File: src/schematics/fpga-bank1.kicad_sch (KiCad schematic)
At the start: 7 parts

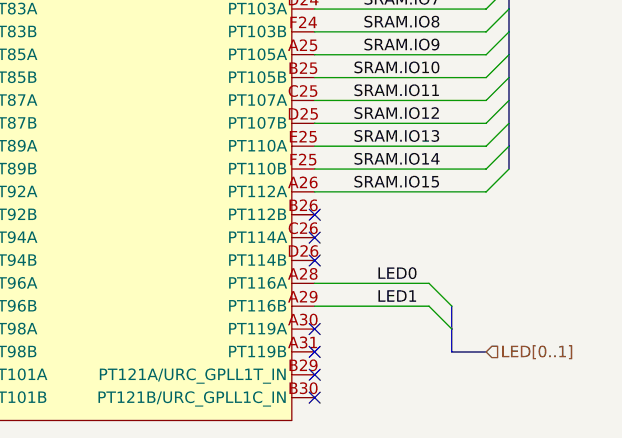
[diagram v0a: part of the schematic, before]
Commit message: Add footprint for the io connector
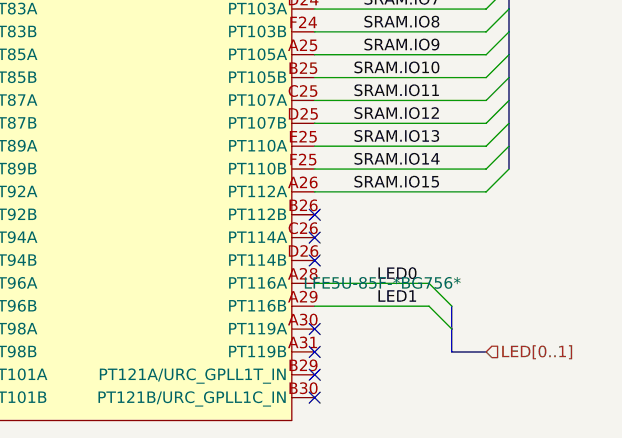
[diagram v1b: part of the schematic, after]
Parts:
- U6: value ~ -> LFE5U-85F-*BG756*
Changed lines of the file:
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@@
 			)
 		)
-		(property "Value" "~"
+		(property "Value" "LFE5U-85F-*BG756*"
 			(at 171.45 133.35 0)
 			(effects

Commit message: Add remaining component footprints (#79)
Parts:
- C54, C55, C56, C57, C58, C59: footprint (none) -> Capacitor_SMD:C_0402_1005Metric
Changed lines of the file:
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@@
 			)
 		)
-		(property "Footprint" ""
+		(property "Footprint" "Capacitor_SMD:C_0402_1005Metric"
 			(at 109.22 35.56 0)
 			(effects
@@
 			)
 		)
-		(property "Footprint" ""
+		(property "Footprint" "Capacitor_SMD:C_0402_1005Metric"
 			(at 161.29 35.56 0)
 			(effects
@@
 			)
 		)
-		(property "Footprint" ""
+		(property "Footprint" "Capacitor_SMD:C_0402_1005Metric"
 			(at 129.54 35.56 0)
 			(effects
@@
 			)
 		)
-		(property "Footprint" ""
+		(property "Footprint" "Capacitor_SMD:C_0402_1005Metric"
 			(at 139.7 35.56 0)
 			(effects
@@
 			)
 		)
-		(property "Footprint" ""
+		(property "Footprint" "Capacitor_SMD:C_0402_1005Metric"
 			(at 119.38 35.56 0)
 			(effects
@@
 			)
 		)
-		(property "Footprint" ""
+		(property "Footprint" "Capacitor_SMD:C_0402_1005Metric"
 			(at 149.86 35.56 0)
 			(effects

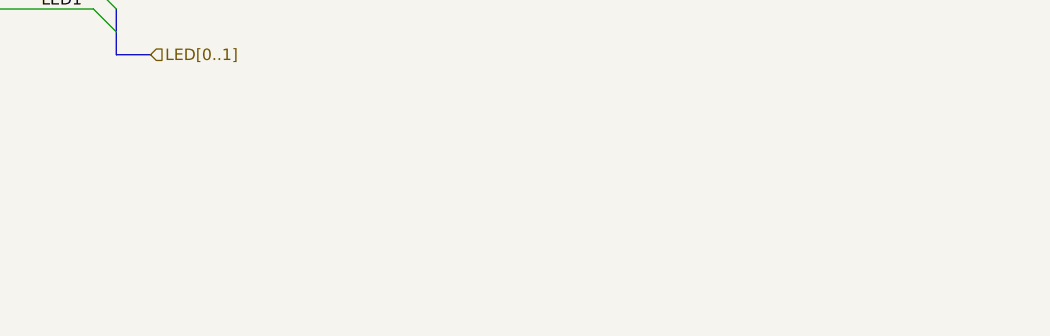
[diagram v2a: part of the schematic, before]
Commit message: Add notes on the schematic
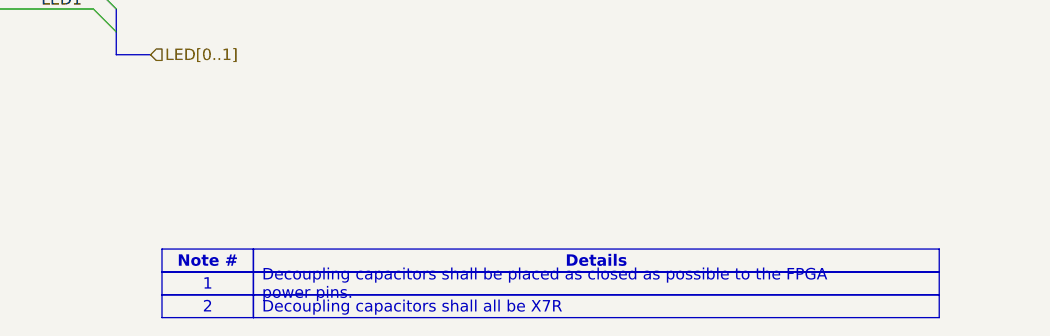
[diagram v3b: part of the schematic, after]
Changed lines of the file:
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@@
 		(comment 3 "${Part Number}")
+	)
+	(text_box "1"
+		(exclude_from_sim no)
+		(at 193.04 165.1 0)
+		(size 10.16 2.54)
+		(margins 0.9525 0.9525 0.9525 0.9525)
+		(stroke
+			(width 0)
+			(type solid)
+			(color 0 0 0 1)
+		)
+		(fill
+			(type none)
+		)
+		(effects
+			(font
+				(face "Arial")
+				(size 1.27 1.27)
+				(color 0 0 0 1)
+			)
+		)
+	)
+	(text_box "Note #"
+		(exclude_from_sim no)
+		(at 193.04 162.56 0)
+		(size 10.16 2.54)
+		(margins 0.9525 0.9525 0.9525 0.9525)
+		(stroke
+			(width 0)
+			(type solid)
+			(color 0 0 0 1)
+		)
+		(fill
+			(type none)
+		)
+		(effects
+			(font
+				(face "Arial")
+				(size 1.27 1.27)
+				(bold yes)
+				(color 0 0 0 1)
+			)
+		)
+	)
+	(text_box "Decoupling capacitors shall be placed as closed as possible to the FPGA power pins."
+		(exclude_from_sim no)
+		(at 203.2 165.1 0)
+		(size 76.2 2.54)
+		(margins 0.9525 0.9525 0.9525 0.9525)
+		(stroke
+			(width 0)
+			(type solid)
+			(color 0 0 0 1)
+		)
+		(fill
+			(type none)
+		)
+		(effects
+			(font
+				(face "Arial")
+				(size 1.27 1.27)
+				(color 0 0 0 1)
+			)
+			(justify left)
+		)
+	)
+	(text_box "Details"
+		(exclude_from_sim no)
+		(at 203.2 162.56 0)
+		(size 76.2 2.54)
+		(margins 0.9525 0.9525 0.9525 0.9525)
+		(stroke
+			(width 0)
+			(type solid)
+			(color 0 0 0 1)
+		)
+		(fill
+			(type none)
+		)
+		(effects
+			(font
+				(face "Arial")
+				(size 1.27 1.27)
+				(bold yes)
+				(color 0 0 0 1)
+			)
+		)
+	)
+	(text_box "Decoupling capacitors shall all be X7R"
+		(exclude_from_sim no)
+		(at 203.2 167.64 0)
+		(size 76.2 2.54)
+		(margins 0.9525 0.9525 0.9525 0.9525)
+		(stroke
+			(width 0)
+			(type solid)
+			(color 0 0 0 1)
+		)
+		(fill
+			(type none)
+		)
+		(effects
+			(font
+				(face "Arial")
+				(size 1.27 1.27)
+				(color 0 0 0 1)
+			)
+			(justify left)
+		)
+	)
+	(text_box "2"
+		(exclude_from_sim no)
+		(at 193.04 167.64 0)
+		(size 10.16 2.54)
+		(margins 0.9525 0.9525 0.9525 0.9525)
+		(stroke
+			(width 0)
+			(type solid)
+			(color 0 0 0 1)
+		)
+		(fill
+			(type none)
+		)
+		(effects
+			(font
+				(face "Arial")
+				(size 1.27 1.27)
+				(color 0 0 0 1)
+			)
+		)
 	)
 	(junction

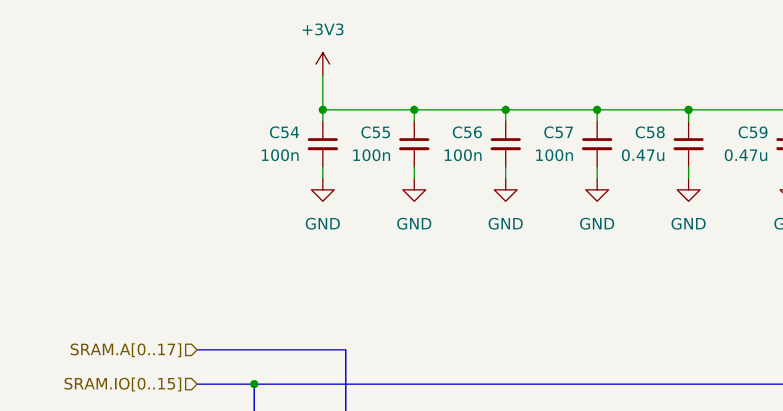
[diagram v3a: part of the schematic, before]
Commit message: Adds decoupling capacitors
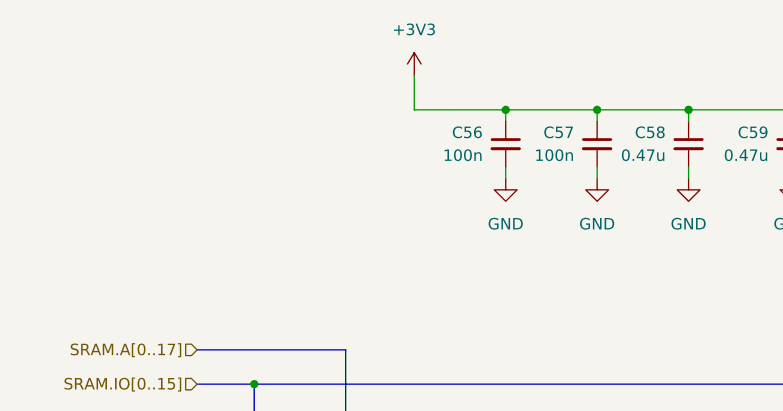
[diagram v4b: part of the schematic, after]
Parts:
- removed C54, C55: 100n, Capacitor_SMD:C_0402_1005Metric, symbol Device:C_Small
- C56, C57, C58, C59: footprint Capacitor_SMD:C_0402_1005Metric -> Capacitor_SMD:C_0201_0603Metric

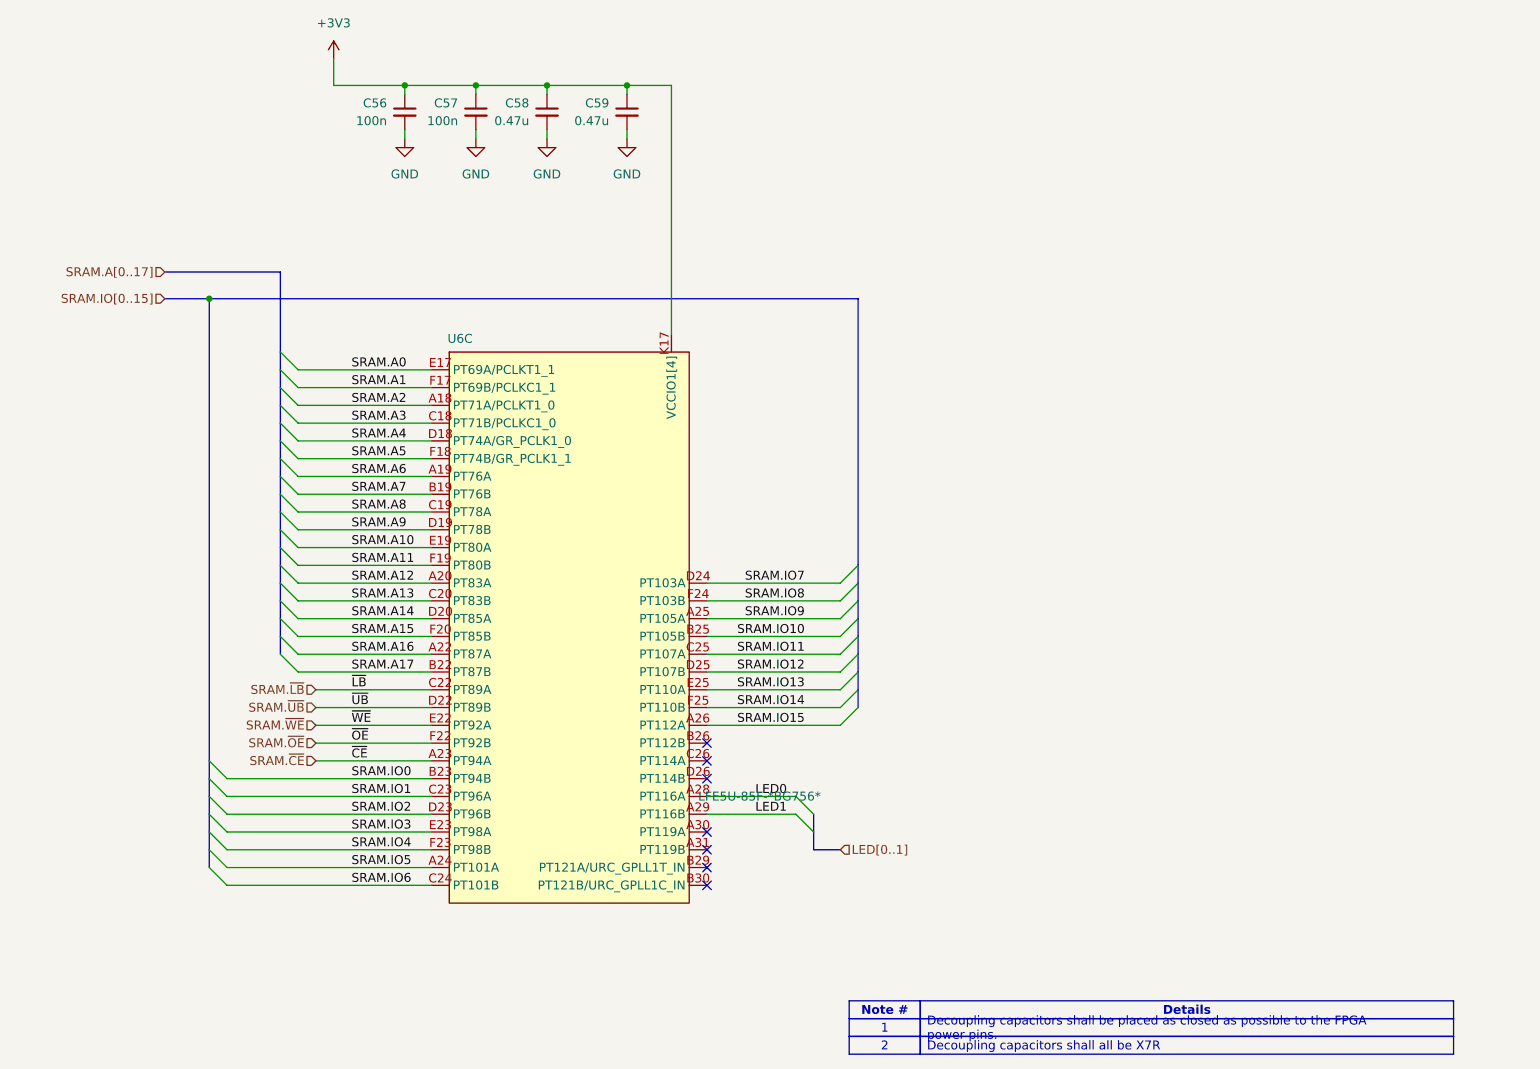
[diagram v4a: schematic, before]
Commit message: Add routing for SRAM
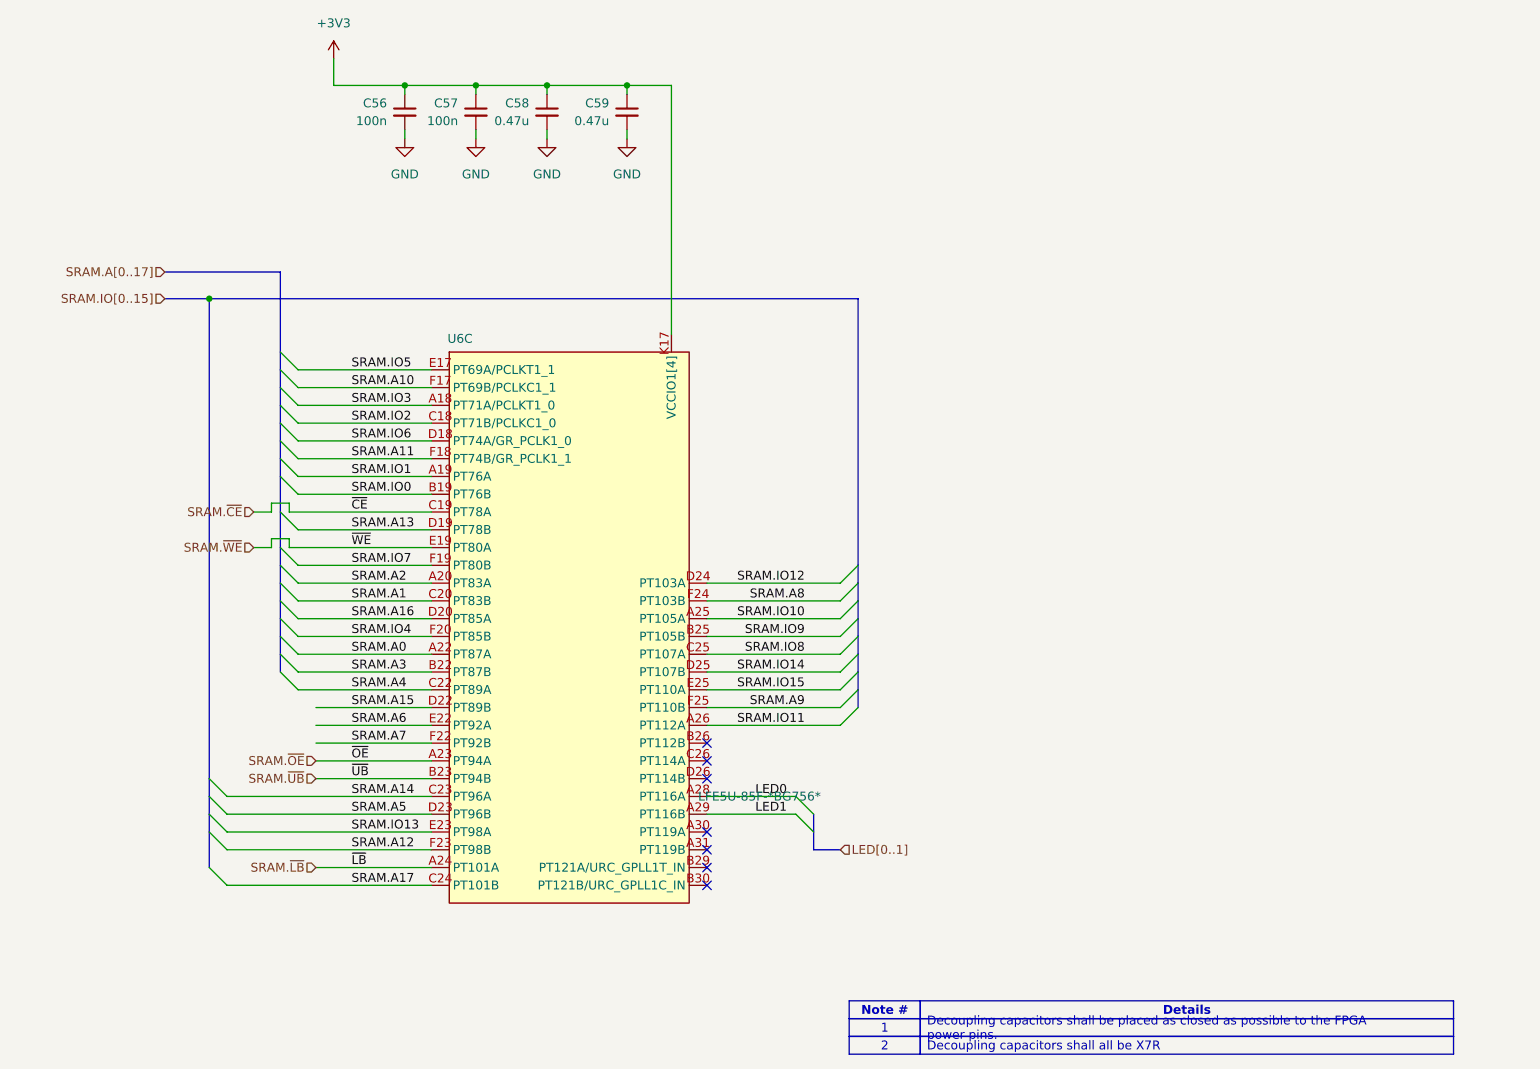
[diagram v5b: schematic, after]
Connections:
- net SRAM.A0: now also U6.A22 (PT87A); no longer U6.E17 (PT69A/PCLKT1_1)
- net SRAM.A1: now also U6.C20 (PT83B); no longer U6.F17 (PT69B/PCLKC1_1)
- net SRAM.A10: now also U6.F17 (PT69B/PCLKC1_1); no longer U6.E19 (PT80A)
- net SRAM.A11: now also U6.F18 (PT74B/GR_PCLK1_1); no longer U6.F19 (PT80B)
- net SRAM.A12: now also U6.F23 (PT98B); no longer U6.A20 (PT83A)
- net SRAM.A13: now also U6.D19 (PT78B); no longer U6.C20 (PT83B)
- net SRAM.A14: now also U6.C23 (PT96A); no longer U6.D20 (PT85A)
- net SRAM.A15: now also U6.D22 (PT89B); no longer U6.F20 (PT85B)
- net SRAM.A16: now also U6.D20 (PT85A); no longer U6.A22 (PT87A)
- net SRAM.A17: now also U6.C24 (PT101B); no longer U6.B22 (PT87B)
- net SRAM.A2: now also U6.A20 (PT83A); no longer U6.A18 (PT71A/PCLKT1_0)
- net SRAM.A3: now also U6.B22 (PT87B); no longer U6.C18 (PT71B/PCLKC1_0)
- net SRAM.A4: now also U6.C22 (PT89A); no longer U6.D18 (PT74A/GR_PCLK1_0)
- net SRAM.A5: now also U6.D23 (PT96B); no longer U6.F18 (PT74B/GR_PCLK1_1)
- net SRAM.A6: now also U6.E22 (PT92A); no longer U6.A19 (PT76A)
- net SRAM.A7: now also U6.F22 (PT92B); no longer U6.B19 (PT76B)
- net SRAM.A8: now also U6.F24 (PT103B); no longer U6.C19 (PT78A)
- net SRAM.A9: now also U6.F25 (PT110B); no longer U6.D19 (PT78B)
- net SRAM.IO0: now also U6.B19 (PT76B); no longer U6.B23 (PT94B)
- net SRAM.IO1: now also U6.A19 (PT76A); no longer U6.C23 (PT96A)
- net SRAM.IO10: now also U6.A25 (PT105A); no longer U6.B25 (PT105B)
- net SRAM.IO11: now also U6.A26 (PT112A); no longer U6.C25 (PT107A)
- net SRAM.IO12: now also U6.D24 (PT103A); no longer U6.D25 (PT107B)
- net SRAM.IO13: now also U6.E23 (PT98A); no longer U6.E25 (PT110A)
- net SRAM.IO14: now also U6.D25 (PT107B); no longer U6.F25 (PT110B)
- net SRAM.IO15: now also U6.E25 (PT110A); no longer U6.A26 (PT112A)
- net SRAM.IO2: now also U6.C18 (PT71B/PCLKC1_0); no longer U6.D23 (PT96B)
- net SRAM.IO3: now also U6.A18 (PT71A/PCLKT1_0); no longer U6.E23 (PT98A)
- net SRAM.IO4: now also U6.F20 (PT85B); no longer U6.F23 (PT98B)
- net SRAM.IO5: now also U6.E17 (PT69A/PCLKT1_1); no longer U6.A24 (PT101A)
- net SRAM.IO6: now also U6.D18 (PT74A/GR_PCLK1_0); no longer U6.C24 (PT101B)
- net SRAM.IO7: now also U6.F19 (PT80B); no longer U6.D24 (PT103A)
- net SRAM.IO8: now also U6.C25 (PT107A); no longer U6.F24 (PT103B)
- net SRAM.IO9: now also U6.B25 (PT105B); no longer U6.A25 (PT105A)
- net SRAM.~{CE}: now also U6.C19 (PT78A); no longer U6.A23 (PT94A)
- net SRAM.~{LB}: now also U6.A24 (PT101A); no longer U6.C22 (PT89A)
- net SRAM.~{OE}: now also U6.A23 (PT94A); no longer U6.F22 (PT92B)
- net SRAM.~{UB}: now also U6.B23 (PT94B); no longer U6.D22 (PT89B)
- net SRAM.~{WE}: now also U6.E19 (PT80A); no longer U6.E22 (PT92A)

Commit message: Route the SRAM data pins
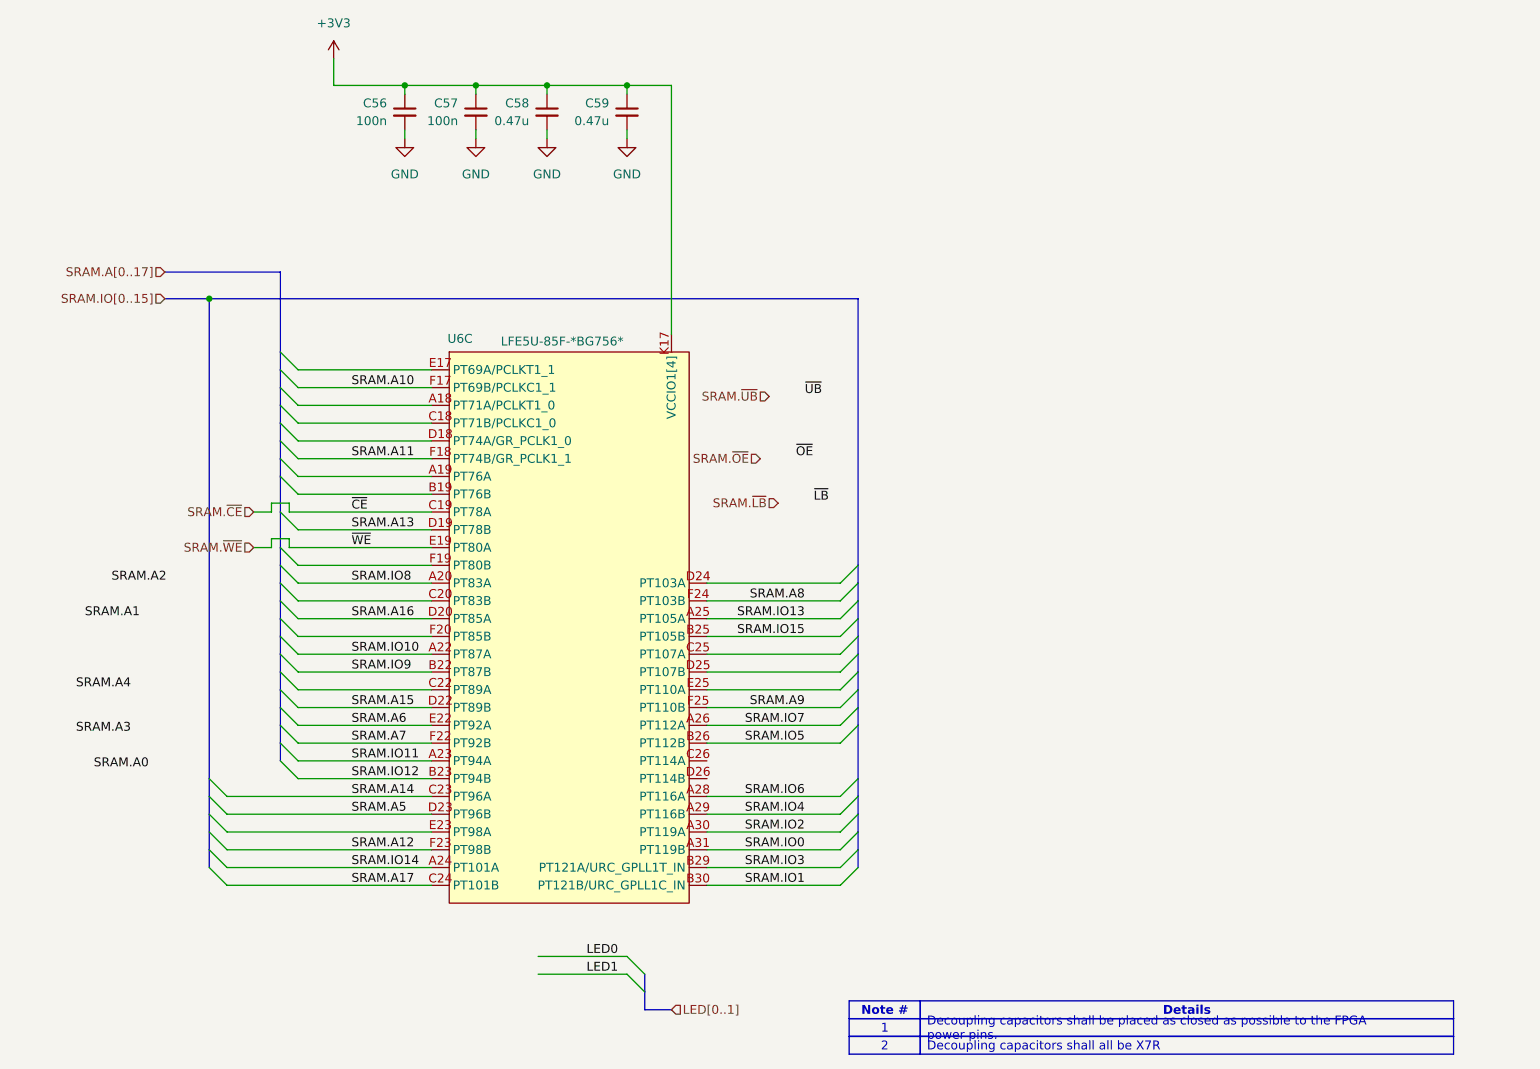
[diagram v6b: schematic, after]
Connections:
- net LED0: no longer U6.A28 (PT116A)
- net LED1: no longer U6.A29 (PT116B)
- net SRAM.A0: no longer U6.A22 (PT87A)
- net SRAM.A1: no longer U6.C20 (PT83B)
- net SRAM.A2: no longer U6.A20 (PT83A)
- net SRAM.A3: no longer U6.B22 (PT87B)
- net SRAM.A4: no longer U6.C22 (PT89A)
- net SRAM.IO0: now also U6.A31 (PT119B); no longer U6.B19 (PT76B)
- net SRAM.IO1: now also U6.B30 (PT121B/URC_GPLL1C_IN); no longer U6.A19 (PT76A)
- net SRAM.IO10: now also U6.A22 (PT87A); no longer U6.A25 (PT105A)
- net SRAM.IO11: now also U6.A23 (PT94A); no longer U6.A26 (PT112A)
- net SRAM.IO12: now also U6.B23 (PT94B); no longer U6.D24 (PT103A)
- net SRAM.IO13: now also U6.A25 (PT105A); no longer U6.E23 (PT98A)
- net SRAM.IO14: now also U6.A24 (PT101A); no longer U6.D25 (PT107B)
- net SRAM.IO15: now also U6.B25 (PT105B); no longer U6.E25 (PT110A)
- net SRAM.IO2: now also U6.A30 (PT119A); no longer U6.C18 (PT71B/PCLKC1_0)
- net SRAM.IO3: now also U6.B29 (PT121A/URC_GPLL1T_IN); no longer U6.A18 (PT71A/PCLKT1_0)
- net SRAM.IO4: now also U6.A29 (PT116B); no longer U6.F20 (PT85B)
- net SRAM.IO5: now also U6.B26 (PT112B); no longer U6.E17 (PT69A/PCLKT1_1)
- net SRAM.IO6: now also U6.A28 (PT116A); no longer U6.D18 (PT74A/GR_PCLK1_0)
- net SRAM.IO7: now also U6.A26 (PT112A); no longer U6.F19 (PT80B)
- net SRAM.IO8: now also U6.A20 (PT83A); no longer U6.C25 (PT107A)
- net SRAM.IO9: now also U6.B22 (PT87B); no longer U6.B25 (PT105B)
- net SRAM.~{LB}: no longer U6.A24 (PT101A)
- net SRAM.~{OE}: no longer U6.A23 (PT94A)
- net SRAM.~{UB}: no longer U6.B23 (PT94B)
- no-connect marks 7 -> 0
